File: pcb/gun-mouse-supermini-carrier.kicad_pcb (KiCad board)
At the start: 2 copper layers, 52 x 82 mm, 21 parts, among them SW1 HW-504 34x26mm, SW2 D2FC-F-7N(20M)

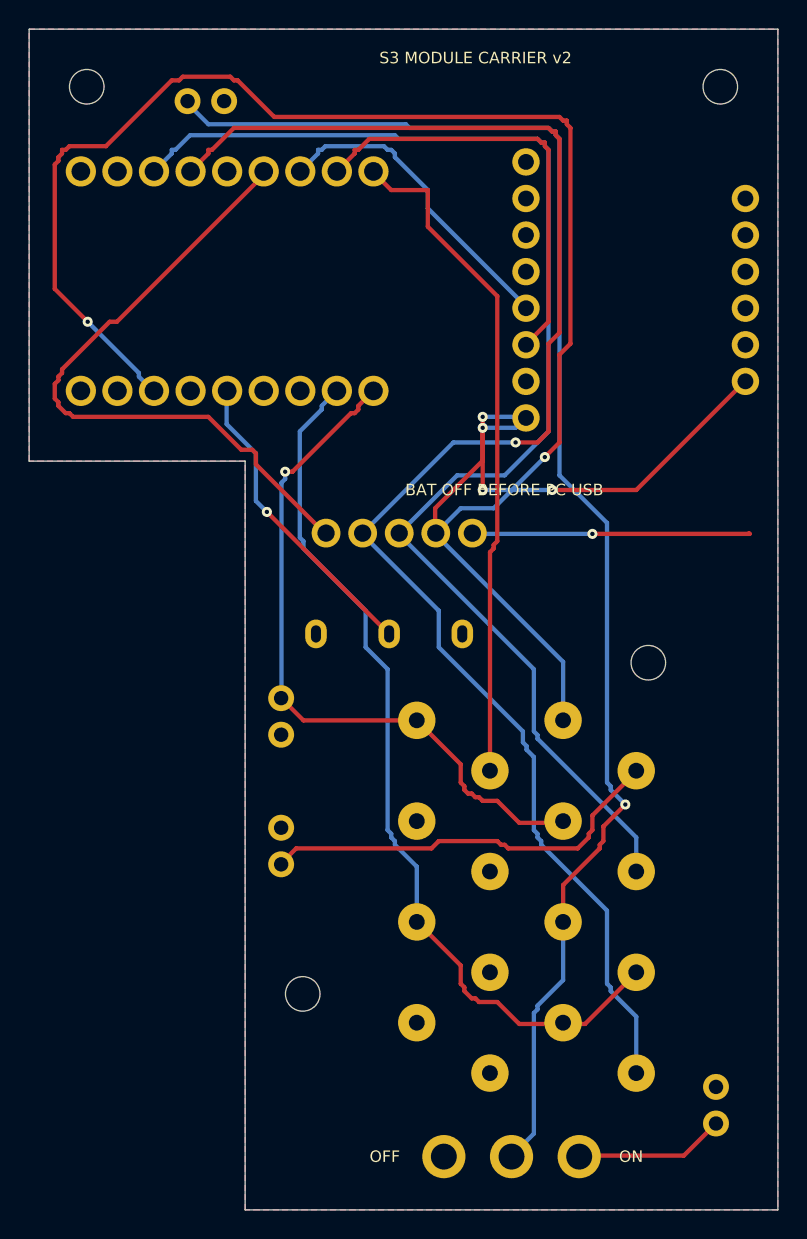
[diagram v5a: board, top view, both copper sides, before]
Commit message: 预留摇杆直插焊孔并同步完整装配模型
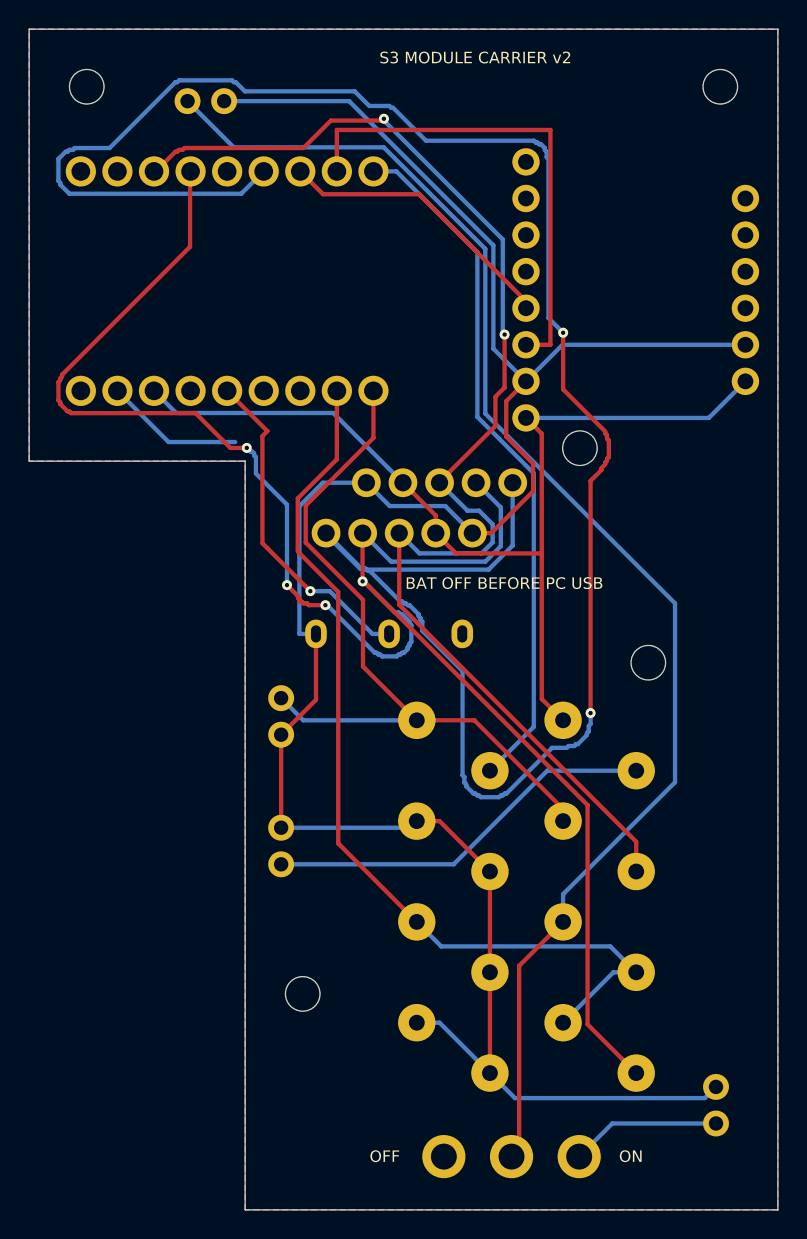
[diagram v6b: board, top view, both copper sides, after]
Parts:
- added SW1_ALT: HW-504直排针备用位, GunMouseHandSolder:SW1_ALT, F.Cu at (33.5, 36.5)
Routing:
- net GND: track 19.4 -> 165.6 mm, vias 1 -> 0
- net JOY_SW: track 45.4 -> 149.8 mm, vias 0 -> 2
- net 3V3: track 151.1 -> 70.7 mm, vias 6 -> 0
- net JOY_Y: track 109.6 -> 123.8 mm, vias 1 -> 4
- net BAT_SW: track 103.1 -> 98.1 mm, vias 1 -> 0
- net SCL: track 30.5 -> 34.3 mm
- net TRIG: track 48.7 -> 51.6 mm, vias 1 -> 0
- net VBAT_ADC: track 62.1 -> 64.6 mm
- net SDA: track 22.3 -> 19.9 mm
- net BTN_R: track 21.6 -> 23.3 mm
- net TOUCH: track 47.0 -> 48.4 mm
- net TOUCH_ELECTRODE: track 28.6 -> 27.4 mm
- net JOY_X: track 92.6 -> 92.1 mm, vias 0 -> 2
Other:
- board text added: "SW1_ALT.1 JOY_SW"
- board text added: "SW1_ALT.2 JOY_Y"
- board text added: "SW1_ALT.3 JOY_X"
- board text added: "SW1_ALT.4 3V3"
- board text added: "SW1_ALT.5 GND"

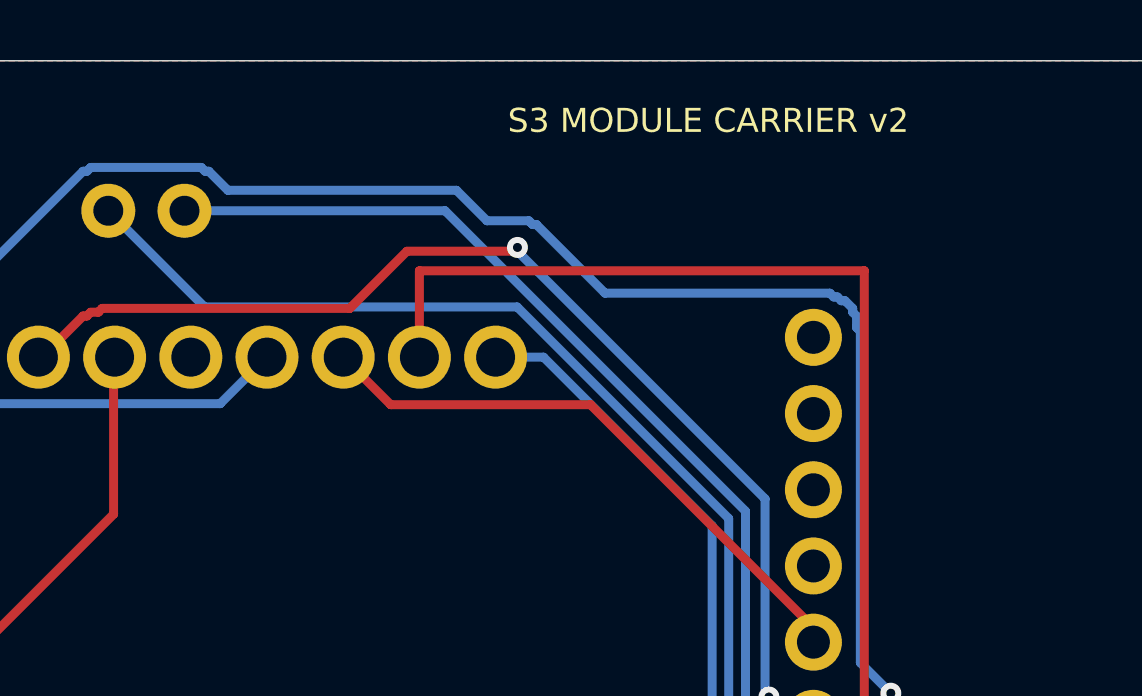
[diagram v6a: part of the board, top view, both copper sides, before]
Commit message: 用共用穿板孔和背侧深梁加强摇杆支座
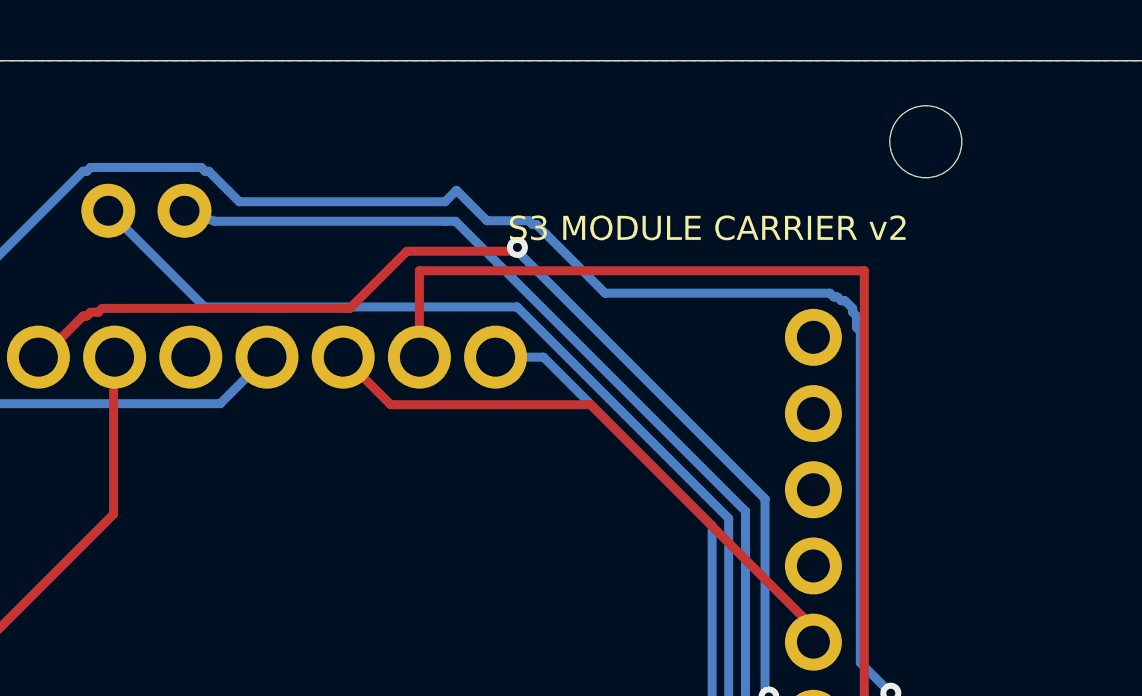
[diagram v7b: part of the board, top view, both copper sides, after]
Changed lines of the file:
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@@
 		(attr through_hole exclude_from_pos_files exclude_from_bom dnp)
 		(pad "" np_thru_hole oval
+			(at -9.75 -28.8)
+			(size 3.6 2.4)
+			(drill oval 3.6 2.4)
+			(layers "*.Cu" "*.Mask")
+			(thermal_bridge_angle 45)
+		)
+		(pad "" np_thru_hole oval
 			(at -9.75 -2.4)
 			(size 3.6 2.4)
@@
 		)
 		(pad "" np_thru_hole circle
+			(at 9.75 -28.8)
+			(size 2.4 2.4)
+			(drill 2.4)
+			(layers "*.Cu" "*.Mask")
+		)
+		(pad "" np_thru_hole circle
 			(at 9.75 -2.4)
 			(size 2.4 2.4)
@@
 	)
 	(gr_text "S3 MODULE CARRIER v2"
-		(at 36 7 0)
+		(at 36 10.6 0)
 		(layer "F.SilkS")
 		(effects
@@
 	)
 	(segment
+		(start 27.5752 10.35)
+		(end 27.2252 10.35)
+		(width 0.3)
+		(layer "B.Cu")
+		(net 5)
+	)
+	(segment
 		(start 39.504 29.46)
 		(end 42.044 26.92)
@@
 	)
 	(segment
-		(start 27.2252 10)
+		(start 19.54 10.35)
 		(end 18.54 10)
 		(width 0.3)
@@
 	)
 	(segment
+		(start 27.2252 10.35)
+		(end 19.54 10.35)
+		(width 0.3)
+		(layer "B.Cu")
+		(net 5)
+	)
+	(segment
 		(start 37.2397 20.0145)
-		(end 27.2252 10)
+		(end 27.5752 10.35)
 		(width 0.3)
 		(layer "B.Cu")
@@
 	)
 	(segment
+		(start 20.368 9.7)
+		(end 27.224 9.7)
+		(width 0.3)
+		(layer "B.Cu")
+		(net 6)
+	)
+	(segment
 		(start 40.052 12.747)
 		(end 40.179 12.874)
@@
 	)
 	(segment
+		(start 27.224 9.7)
+		(end 27.606 9.318)
+		(width 0.3)
+		(layer "B.Cu")
+		(net 6)
+	)
+	(segment
 		(start 28.495 42.592)
 		(end 28.368 42.465)
@@
 	(segment
 		(start 19.986 9.318)
-		(end 27.606 9.318)
+		(end 20.368 9.7)
 		(width 0.3)
 		(layer "B.Cu")
@@
 	)
 	(zone
+		(net 0)
+		(net_name "")
+		(layer "F.Cu")
+		(name "JOY_SCREW_HEAD_JOY_SHARED_FAR_R")
+		(hatch edge 0.5)
+		(connect_pads
+			(clearance 0)
+		)
+		(min_thickness 0.25)
+		(filled_areas_thickness no)
+		(keepout
+			(tracks not_allowed)
+			(vias not_allowed)
+			(pads allowed)
+			(copperpour not_allowed)
+			(footprints allowed)
+		)
+		(placement
+			(enabled no)
+			(sheetname "")
+		)
+		(fill
+			(thermal_gap 0.5)
+			(thermal_bridge_width 0.5)
+		)
+		(polygon
+			(pts
+				(xy 24.35 5.388871) (xy 24.800878 5.433278) (xy 25.23443 5.564795) (xy 25.633994 5.778366) (xy 25.984214 6.065785)
+				(xy 26.271633 6.416005) (xy 26.485204 6.815569) (xy 26.616721 7.249121) (xy 26.661128 7.7) (xy 26.616721 8.150878)
+				(xy 26.485204 8.58443) (xy 26.271633 8.983994) (xy 25.984214 9.334214) (xy 25.633994 9.621633) (xy 25.23443 9.835204)
+				(xy 24.800878 9.966721) (xy 24.35 10.011128) (xy 23.15 10.011128) (xy 22.699121 9.966721) (xy 22.265569 9.835204)
+				(xy 21.866005 9.621633) (xy 21.515785 9.334214) (xy 21.228366 8.983994) (xy 21.014795 8.58443) (xy 20.883278 8.150878)
+				(xy 20.838871 7.7) (xy 20.883278 7.249121) (xy 21.014795 6.815569) (xy 21.228366 6.416005) (xy 21.515785 6.065785)
+				(xy 21.866005 5.778366) (xy 22.265569 5.564795) (xy 22.699121 5.433278) (xy 23.15 5.388871)
+			)
+		)
+	)
+	(zone
 		(net 5)
 		(net_name "GND")
@@
 			)
 		)
+	)
+	(zone
+		(net 0)
+		(net_name "")
+		(layer "F.Cu")
+		(name "JOY_SCREW_HEAD_JOY_SHARED_FAR_L")
+		(hatch edge 0.5)
+		(connect_pads
+			(clearance 0)
+		)
+		(min_thickness 0.25)
+		(filled_areas_thickness no)
+		(keepout
+			(tracks not_allowed)
+			(vias not_allowed)
+			(pads allowed)
+			(copperpour not_allowed)
+			(footprints allowed)
+		)
+		(placement
+			(enabled no)
+			(sheetname "")
+		)
+		(fill
+			(thermal_gap 0.5)
+			(thermal_bridge_width 0.5)
+		)
+		(polygon
+			(pts
+				(xy 43.25 5.388871) (xy 43.700878 5.433278) (xy 44.13443 5.564795) (xy 44.533994 5.778366) (xy 44.884214 6.065785)
+				(xy 45.171633 6.416005) (xy 45.385204 6.815569) (xy 45.516721 7.249121) (xy 45.561128 7.7) (xy 45.516721 8.150878)
+				(xy 45.385204 8.58443) (xy 45.171633 8.983994) (xy 44.884214 9.334214) (xy 44.533994 9.621633) (xy 44.13443 9.835204)
+				(xy 43.700878 9.966721) (xy 43.25 10.011128) (xy 42.799121 9.966721) (xy 42.365569 9.835204) (xy 41.966005 9.621633)
+				(xy 41.615785 9.334214) (xy 41.328366 8.983994) (xy 41.114795 8.58443) (xy 40.983278 8.150878) (xy 40.938871 7.7)
+				(xy 40.983278 7.249121) (xy 41.114795 6.815569) (xy 41.328366 6.416005) (xy 41.615785 6.065785)
+				(xy 41.966005 5.778366) (xy 42.365569 5.564795) (xy 42.799121 5.433278)
+			)
+		)
